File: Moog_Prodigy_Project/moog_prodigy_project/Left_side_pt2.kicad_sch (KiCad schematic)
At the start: 61 parts, among them Q1 CA3046, Q15 BC549, Q2 CA3046, Q4 CA3046, Q6 BC549, SW1 Switch_4x4, SW4 Switch_4x4, U2A1 OPA134, U2B3 OPA134, U5 NE5532, U6 LT1011CN8, U7 AD8066ARM, U8 NE5532

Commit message: Spajanje projekta final 1
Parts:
- removed C1, C9: 47p, Capacitor_THT:CP_Radial_D5.0mm_P2.50mm, symbol Device:C
- removed C10, C5, C6: 10n, Capacitor_THT:C_Disc_D3.8mm_W2.6mm_P2.50mm, symbol Device:C
- removed C11: 0.5n, Capacitor_THT:C_Disc_D3.8mm_W2.6mm_P2.50mm, symbol Device:C
- removed C12: 0.01n, Capacitor_THT:C_Disc_D3.8mm_W2.6mm_P2.50mm, symbol Device:C
- removed C2: 0.01, Capacitor_THT:C_Disc_D3.8mm_W2.6mm_P2.50mm, symbol Device:C
- removed C7: 1000n, Capacitor_THT:CP_Radial_D5.0mm_P2.50mm, symbol Device:C
- removed C8: 1n, Capacitor_THT:C_Disc_D3.8mm_W2.6mm_P2.50mm, symbol Device:C
- removed Q1, Q2, Q4, UI2: CA3046, CA3046:DIL14, symbol CA3046:CA3046
- removed Q14: ~, BF256C:TO92127P478H483-3, symbol Transistor_FET:BF256C
- removed Q15, Q6: BC549, Package_TO_SOT_THT:TO-92_Inline, symbol Transistor_BJT:BC549
- removed R1, R2: 2M, Resistor_THT:R_Axial_DIN0207_L6.3mm_D2.5mm_P7.62mm_Horizontal, symbol Device:R
- removed R10: 1K, Resistor_THT:R_Axial_DIN0207_L6.3mm_D2.5mm_P7.62mm_Horizontal, symbol Device:R
- removed R11: 12K, Resistor_THT:R_Axial_DIN0207_L6.3mm_D2.5mm_P7.62mm_Horizontal, symbol Device:R
- removed R12, R51, R8: 100K, Resistor_THT:R_Axial_DIN0207_L6.3mm_D2.5mm_P7.62mm_Horizontal, symbol Device:R
- removed R13: 63K4, Resistor_THT:R_Axial_DIN0207_L6.3mm_D2.5mm_P7.62mm_Horizontal, symbol Device:R
- removed R14, R7: 500, Resistor_THT:R_Axial_DIN0207_L6.3mm_D2.5mm_P7.62mm_Horizontal, symbol Device:R_Potentiometer
- removed R15: 3K, Resistor_THT:R_Axial_DIN0207_L6.3mm_D2.5mm_P7.62mm_Horizontal, symbol Device:R
- removed R16: 22K, Resistor_THT:R_Axial_DIN0207_L6.3mm_D2.5mm_P7.62mm_Horizontal, symbol Device:R
- removed R17: 15K, Resistor_THT:R_Axial_DIN0207_L6.3mm_D2.5mm_P7.62mm_Horizontal, symbol Device:R
- removed R18: 470, Resistor_THT:R_Axial_DIN0207_L6.3mm_D2.5mm_P7.62mm_Horizontal, symbol Device:R
- removed R3, R42, R54: 10K, Resistor_THT:R_Axial_DIN0207_L6.3mm_D2.5mm_P7.62mm_Horizontal, symbol Device:R_Potentiometer
- removed R4: 120K, Resistor_THT:R_Axial_DIN0207_L6.3mm_D2.5mm_P7.62mm_Horizontal, symbol Device:R
- removed R40: 20K, Resistor_THT:R_Axial_DIN0207_L6.3mm_D2.5mm_P7.62mm_Horizontal, symbol Device:R
- removed R41, R43: 2K, Resistor_THT:R_Axial_DIN0207_L6.3mm_D2.5mm_P7.62mm_Horizontal, symbol Device:R
- removed R44: 1M, Resistor_THT:R_Axial_DIN0207_L6.3mm_D2.5mm_P7.62mm_Horizontal, symbol Device:R
- removed R45, R46, R47, R48, R49, R50, R52, R55, R56: 10K, Resistor_THT:R_Axial_DIN0207_L6.3mm_D2.5mm_P7.62mm_Horizontal, symbol Device:R
- removed R5, R6: 100, Resistor_THT:R_Axial_DIN0207_L6.3mm_D2.5mm_P7.62mm_Horizontal, symbol Device:R
- removed R53: 51M, Resistor_THT:R_Axial_DIN0207_L6.3mm_D2.5mm_P7.62mm_Horizontal, symbol Device:R
- removed R57: 18K2, Resistor_THT:R_Axial_DIN0207_L6.3mm_D2.5mm_P7.62mm_Horizontal, symbol Device:R
- removed R9: 4K75, Resistor_THT:R_Axial_DIN0207_L6.3mm_D2.5mm_P7.62mm_Horizontal, symbol Device:R
- removed SW1, SW4: Switch_4x4, SLW-1575662-5A-S-D_Switch_4x4:SW_SLW-1575662-5A-S-D, symbol Power_supply:SW_Slide_DPDT_4x4
- removed U2A1, U2B3: OPA134, OPA134PA:DIP794W45P254L959H508Q8, symbol Amplifier_Operational:OPA134
- removed U5, U8: NE5532, NE5532AP:DIP794W45P254L1016H508Q8, symbol Amplifier_Operational:NE5532
- removed U6: LT1011CN8, Package_DIP:DIP-8_W7.62mm_Socket, symbol LM393BIPWR:LM393BIPWR
- removed U7: AD8066ARM, AD8066ARM:SOP65P490X110-8N, symbol AD8066ARM:AD8066ARM
- added C13, C16, C17, C18, C4: 10n, Capacitor_THT:C_Disc_D3.8mm_W2.6mm_P2.50mm, symbol Device:C
- added C14: 1n, Capacitor_THT:C_Disc_D3.8mm_W2.6mm_P2.50mm, symbol Device:C
- added C15, C3: 47p, Capacitor_THT:CP_Radial_D5.0mm_P2.50mm, symbol Device:C
- added C19: 500p, Capacitor_THT:CP_Radial_D5.0mm_P2.50mm, symbol Device:C
- added C20: 0.01n, Capacitor_THT:C_Disc_D3.8mm_W2.6mm_P2.50mm, symbol Device:C
- added LED1: ~, WP7113LGD:LED_WP7113LGD, symbol Device:LED_DIODA
- added Q1, Q2, UI3: CA3046, CA3046:DIL14, symbol CA3046:CA3046
- added Q11: BC107, Package_TO_SOT_THT:TO-18-3, symbol Transistor_BJT:BC107
- added Q13, Q16: ~, BF256C:TO92127P478H483-3, symbol Transistor_FET:BF256C
- added Q17: BC549, Package_TO_SOT_THT:TO-92_Inline, symbol Transistor_BJT:BC549
- added R171, R21, R23, R63, R69: 10K, Resistor_THT:R_Axial_DIN0207_L6.3mm_D2.5mm_P7.62mm_Horizontal, symbol Device:R_Potentiometer
- added R19, R20, R61: 1M, Resistor_THT:R_Axial_DIN0207_L6.3mm_D2.5mm_P7.62mm_Horizontal, symbol Device:R
- added R22: 82K, Resistor_THT:R_Axial_DIN0207_L6.3mm_D2.5mm_P7.62mm_Horizontal, symbol Device:R
- added R24: 120K, Resistor_THT:R_Axial_DIN0207_L6.3mm_D2.5mm_P7.62mm_Horizontal, symbol Device:R
- added R25: 10, Resistor_THT:R_Axial_DIN0207_L6.3mm_D2.5mm_P7.62mm_Horizontal, symbol Device:R
- added R26, R27: 100, Resistor_THT:R_Axial_DIN0207_L6.3mm_D2.5mm_P7.62mm_Horizontal, symbol Device:R
- added R28, R35: 500, Resistor_THT:R_Axial_DIN0207_L6.3mm_D2.5mm_P7.62mm_Horizontal, symbol Device:R_Potentiometer
- added R30: 4K75, Resistor_THT:R_Axial_DIN0207_L6.3mm_D2.5mm_P7.62mm_Horizontal, symbol Device:R
- added R31, R76: 1K, Resistor_THT:R_Axial_DIN0207_L6.3mm_D2.5mm_P7.62mm_Horizontal, symbol Device:R
- added R32: 12KΩ, Resistor_THT:R_Axial_DIN0207_L6.3mm_D2.5mm_P7.62mm_Horizontal, symbol Device:R
- added R33: 100KΩ, Resistor_THT:R_Axial_DIN0207_L6.3mm_D2.5mm_P7.62mm_Horizontal, symbol Device:R
- added R34, R73: 100K, Resistor_THT:R_Axial_DIN0207_L6.3mm_D2.5mm_P7.62mm_Horizontal, symbol Device:R
- added R36: 3K, Resistor_THT:R_Axial_DIN0207_L6.3mm_D2.5mm_P7.62mm_Horizontal, symbol Device:R
- added R37: 22K, Resistor_THT:R_Axial_DIN0207_L6.3mm_D2.5mm_P7.62mm_Horizontal, symbol Device:R
- added R38: 15K, Resistor_THT:R_Axial_DIN0207_L6.3mm_D2.5mm_P7.62mm_Horizontal, symbol Device:R
- added R39: 470, Resistor_THT:R_Axial_DIN0207_L6.3mm_D2.5mm_P7.62mm_Horizontal, symbol Device:R
- added R58: 20K, Resistor_THT:R_Axial_DIN0207_L6.3mm_D2.5mm_P7.62mm_Horizontal, symbol Device:R
- added R59: 560, Resistor_THT:R_Axial_DIN0207_L6.3mm_D2.5mm_P7.62mm_Horizontal, symbol Device:R
- added R60: 2K, Resistor_THT:R_Axial_DIN0207_L6.3mm_D2.5mm_P7.62mm_Horizontal, symbol Device:R
- added R62, R64, R65, R66, R67, R68, R70, R71, R74, R75: 10K, Resistor_THT:R_Axial_DIN0207_L6.3mm_D2.5mm_P7.62mm_Horizontal, symbol Device:R
- added R72: 5.1M, Resistor_THT:R_Axial_DIN0207_L6.3mm_D2.5mm_P7.62mm_Horizontal, symbol Device:R
- added S4-1, S4-2: SW_SPST, L101011ML04Q_1x1:SW_L101011ML04Q, symbol Switch:SW_SPST
- added SW2, SW5: Switch_4x4, SLW-1575662-5A-S-D_Switch_4x4:SW_SLW-1575662-5A-S-D, symbol Power_supply:SW_Slide_DPDT_4x4
- added SW3: SW_Slide_DPDT_3x3, CL-SB-22A-02T_3x3:SW_CL-SB-22A-02T, symbol Switch:SW_Slide_DPDT
- added U1: NE5532, NE5532AP:DIP794W45P254L1016H508Q8, symbol Amplifier_Operational:NE5532
- added U10: AD8066ARM, AD8066ARM:SOP65P490X110-8N, symbol AD8066ARM:AD8066ARM
- added U2B1, U4B1: OPA134, OPA134PA:DIP794W45P254L959H508Q8, symbol Amplifier_Operational:OPA134
- added U9: LT1011CN8, Package_DIP:DIP-8_W7.62mm_Socket, symbol LM393BIPWR:LM393BIPWR
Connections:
- net +12V: now also C16.2, Q1.8, R171.1, R21.1, R23.1, R33.1, R34.1, R58.2, R70.2, SW2.2 (B), SW2.4 (D), U10.4, U2B1.7 (V+), U4B1.7 (V+), U9.8
- net -12V: now also C17.1, Q11.1 (E), R171.3, R21.3, R23.3, R32.1, R38.1, S4-1.2 (B), SW3.6 (C), U10.8, U2B1.4 (V-), U4B1.4 (V-), U9.4
- net Flag_ka_U6A: now also SW3.4 (A)
- net GND: now also C13.1, C16.1, C17.2, C18.1, C19.1, Q1.6, Q2.13, R26.2, R27.1, R31.1, R36.2, R59.2, R62.2, R69.3, R74.2, R75.1, U2B1.3 (+)
- new net: Q2.12, R33.2, U4B1.3 (+)
- new net: R21.2, R22.1
- new net: R22.2, R24.2, R25.1, R26.1, UI3.2
- new net: R59.1, R76.2
- new net: C15.1, Q16.2 (G), R60.1, R61.1, U9.1
- new net: C15.2, R61.2, R62.1, U9.3
- new net: Q17.3 (E), R64.1, R73.2, R74.1, SW5.1 (A), U10.2
- new net: R64.2, U9.2
- new net: R28.1, R28.2, R30.2
- new net: R27.2, R28.3, UI3.4
- new net: C14.1, Q13.3 (S), Q16.1 (D), R63.1, R63.2
- new net: C14.2, Q13.1 (D), Q16.3 (S), R60.2, U1.1, U1.2 (-)
- new net: C13.2, C18.2, R58.1, R75.2, U1.3 (+), U9.6
- new net: Q13.2 (G), SW3.5 (B)
- new net: Q17.1 (C), R65.1, R67.1
- new net: C19.2, R67.2, U1.5 (+)
- new net: R66.2, R68.1, U1.6 (-)
- new net: R68.2, R69.1, SW5.6 (F), U1.7
- new net: LED1.1, S4-1.1 (A)
- new net: C4.2, R37.1, U4B1.6
- new net: Q11.2 (B), R37.2, R38.2
- new net: R25.2, SW3.3 (C)
- new net: Q1.10, R31.2, R32.2
- new net: R63.3, U10.3, UI3.1
- new net: C3.1, U2B1.6, UI3.3
- new net: C3.2, R20.2, SW2.5 (E), U2B1.2 (-), UI3.5
- new net: C4.1, R35.2, U4B1.2 (-)
- new net: R65.2, R66.1
- new net: R35.3, R36.1
- new net: LED1.2, S4-2.1 (A)
- new net: R76.1, S4-2.2 (B)
- new net: C20.1, R71.1, R72.2, U9.7
- new net: R70.1, R71.2, SW5.4 (D)
- new net: R34.2, R35.1
- new net: R19.1, R20.1, SW2.3 (C)
- new net: Q17.2 (B), U10.1
- new net: R19.2, SW2.1 (A), SW2.6 (F)
- new net: R171.2, SW3.2 (B)
- new net: Q11.3 (C), R39.1
- new net: Q1.7, R39.2
- new net: R23.2, R24.1
- new net: C20.2, R72.1, R73.1, U9.5
- new net: SW5.2 (B), SW5.3 (C), SW5.7 (G)
- new net Diodna zastita izlaz iz R86: R30.1
- new net Flag_ka_R94: R69.2
- new net Ulaz_na_diodnu_zastitu: SW3.1 (A)
- no-connect marks 9 -> 11
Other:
- note added: "HI END ADJUST"
- note added: "INTERVAL"
- note added: "OSC 2 FREQ TRIM"
- note added: "OSC 2 LEVEL"
- note added: "OSC 2 SCALE TRIM"
- note added: "PITCH (SYNC)"
- note added: "SYNC SWITCH"
- note removed: "OSC 1 CHIP TEMP TRIM"
- note removed: "OSC 1 FREQ TRIM"
- note removed: "OSC 1 HIGH END TRIM"
- note removed: "OSC 1 LEVEL"
- note removed: "OSC 1 SCALE TRIM"
- note removed: "Q2"
- note removed: "Q3"

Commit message: PCB priprema i fix gresaka
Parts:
- added unit 3 of U1
- LED1: value ~ -> Led_dioda; footprint WP7113LGD:LED_WP7113LGD -> LED_THT:LED_D5.0mm
- R21, R63: footprint Resistor_THT:R_Axial_DIN0207_L6.3mm_D2.5mm_P7.62mm_Horizontal -> Potentiometer_THT:Potentiometer_ACP_CA9-V10_Vertical
- RV171: renamed from R171; footprint Resistor_THT:R_Axial_DIN0207_L6.3mm_D2.5mm_P7.62mm_Horizontal -> Potentiometer_THT:Potentiometer_Bourns_3339P_Vertical_HandSoldering
- RV23: renamed from R23; footprint Resistor_THT:R_Axial_DIN0207_L6.3mm_D2.5mm_P7.62mm_Horizontal -> Potentiometer_THT:Potentiometer_Bourns_3339P_Vertical_HandSoldering
- RV28: renamed from R28; footprint Resistor_THT:R_Axial_DIN0207_L6.3mm_D2.5mm_P7.62mm_Horizontal -> Potentiometer_THT:Potentiometer_Bourns_3339P_Vertical_HandSoldering
- RV35: renamed from R35; footprint Resistor_THT:R_Axial_DIN0207_L6.3mm_D2.5mm_P7.62mm_Horizontal -> Potentiometer_THT:Potentiometer_Bourns_3339P_Vertical_HandSoldering
- RV69: renamed from R69; footprint Resistor_THT:R_Axial_DIN0207_L6.3mm_D2.5mm_P7.62mm_Horizontal -> Potentiometer_THT:Potentiometer_Bourns_3339P_Vertical_HandSoldering
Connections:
- net +12V: now also U1.8 (V+)
- net -12V: now also U1.4 (V-)

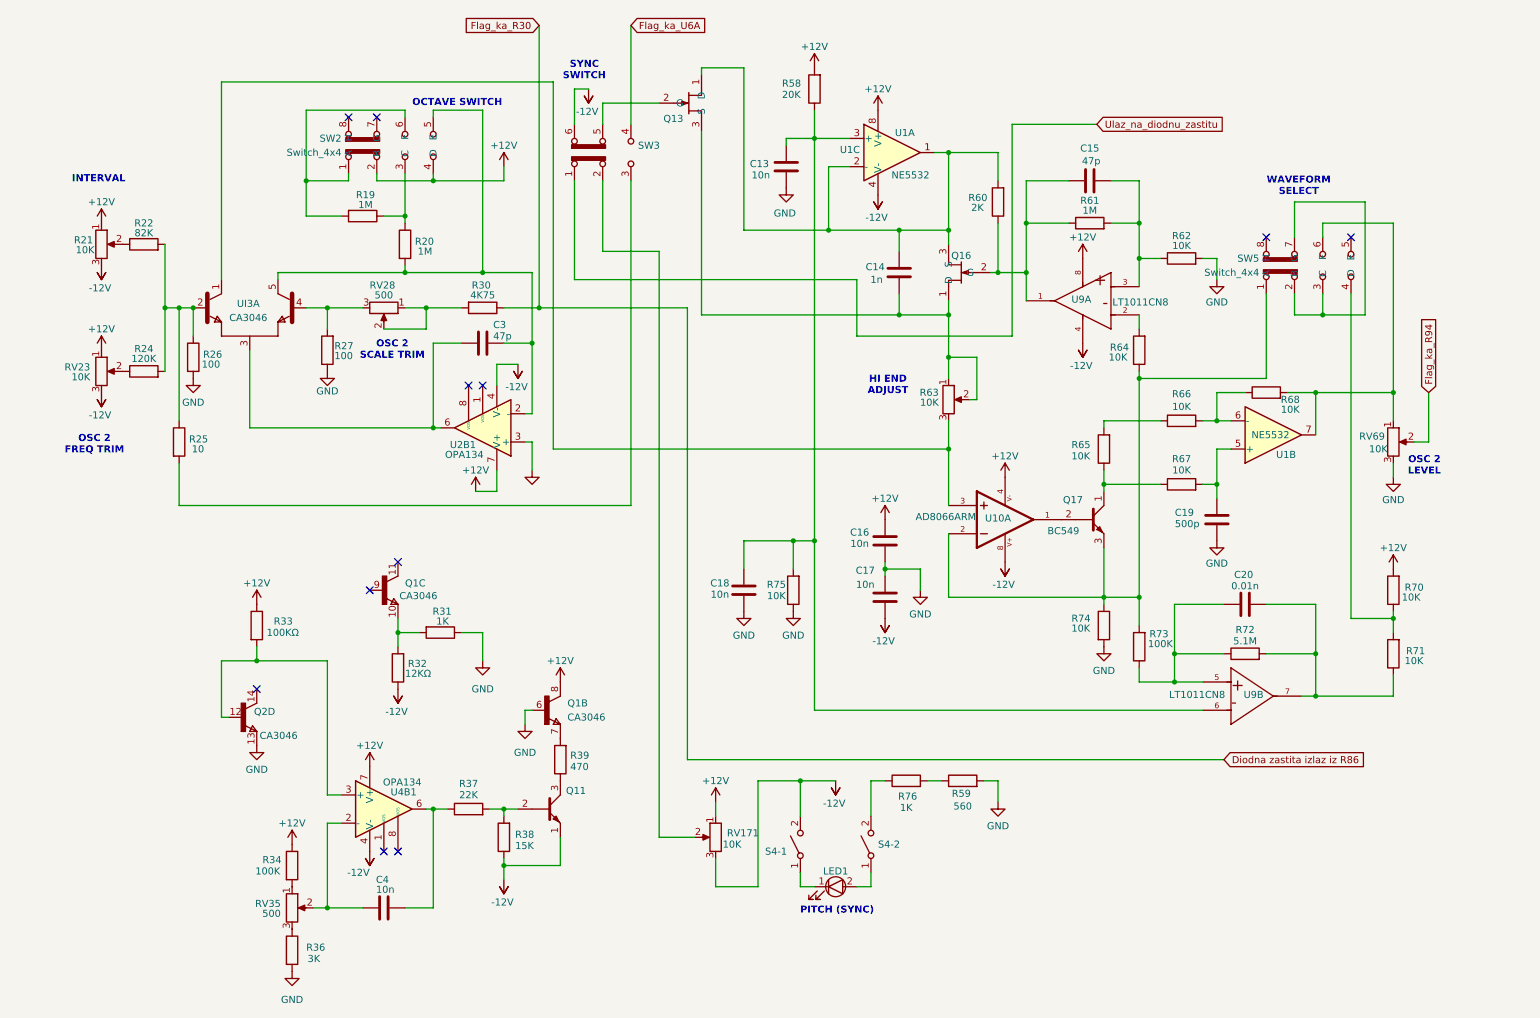
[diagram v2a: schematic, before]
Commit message: problemi sa ca3096, multiplicirani footprintovi
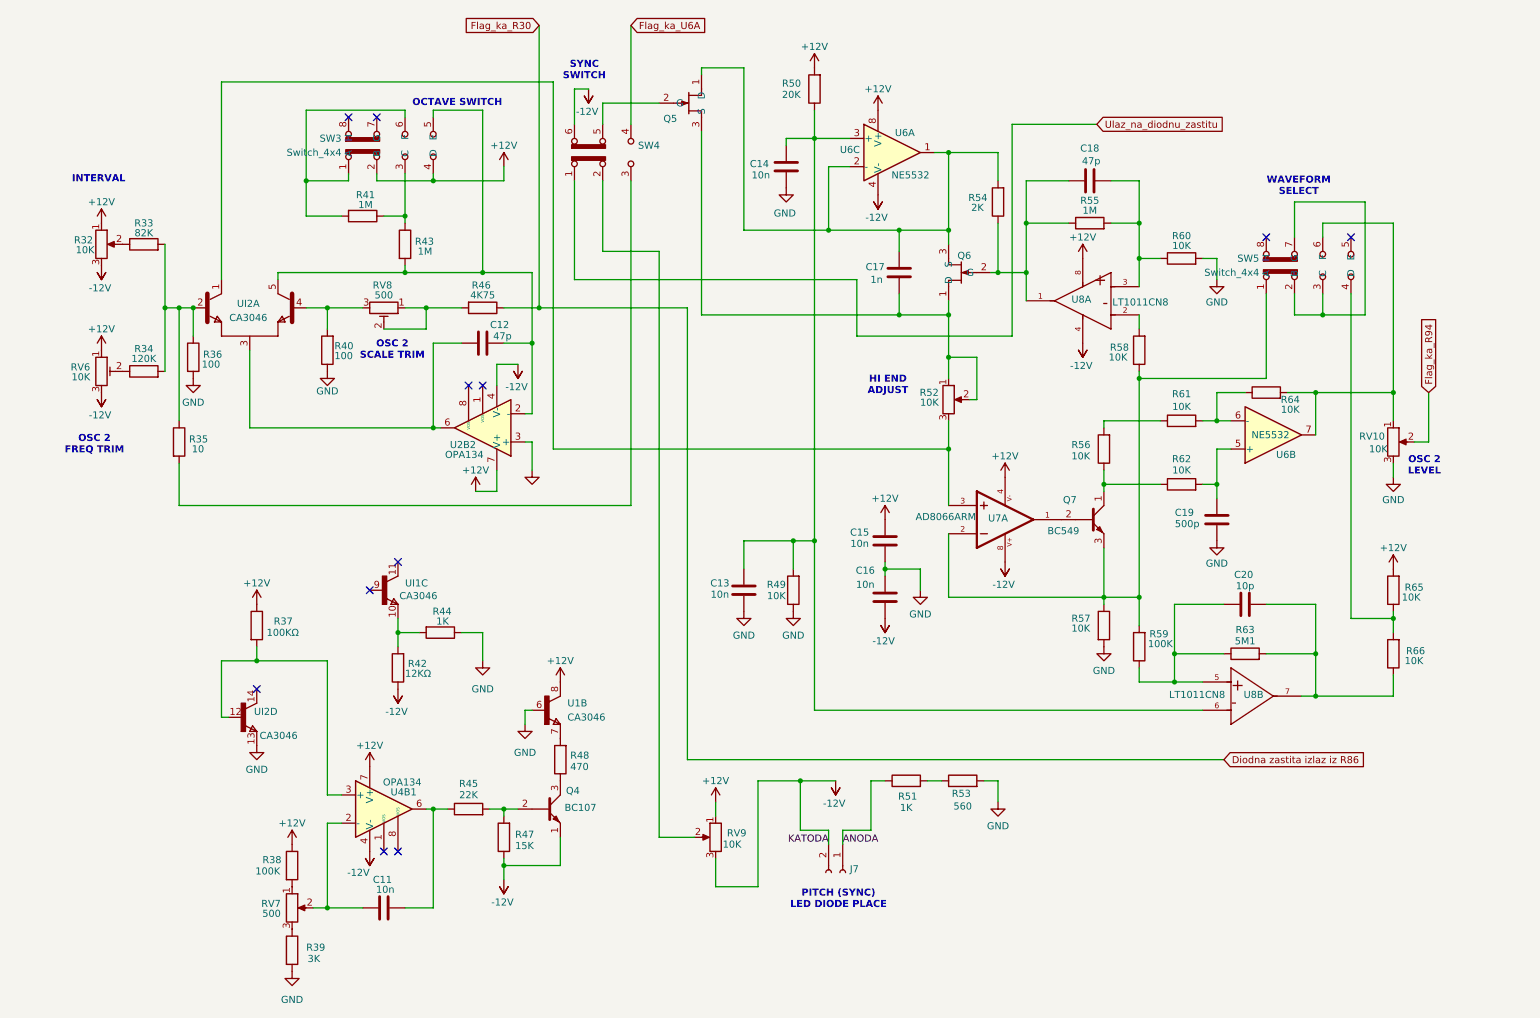
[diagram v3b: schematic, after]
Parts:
- removed LED1: Led_dioda, LED_THT:LED_D5.0mm, symbol Device:LED_DIODA
- removed S4-1, S4-2: SW_SPST, L101011ML04Q_1x1:SW_L101011ML04Q, symbol Switch:SW_SPST
- added J7: Conn_01x02_Socket, Connector_PinSocket_2.54mm:PinSocket_1x02_P2.54mm_Vertical, symbol Connector:Conn_01x02_Socket
- C20: value 0.01n -> 10p
- R63: renamed from R72; value 5.1M -> 5M1
- RV6: renamed from RV23; symbol Device:R_Potentiometer -> Device:R_Potentiometer_Trim
- RV8: renamed from RV28; symbol Device:R_Potentiometer -> Device:R_Potentiometer_Trim
- SW4: renamed from SW3; footprint CL-SB-22A-02T_3x3:SW_CL-SB-22A-02T -> Button_Switch_THT:SW_CK_JS202011CQN_DPDT_Straight
- U7: renamed from U10; footprint AD8066ARM:SOP65P490X110-8N -> Package_DIP:DIP-8_W7.62mm_Socket
- renumbered C4 to C11, C3 to C12, C18 to C13, C13 to C14, C16 to C15, C17 to C16, C14 to C17, C15 to C18, Q11 to Q4, Q13 to Q5, Q16 to Q6, Q17 to Q7, R21 to R32, R22 to R33, R24 to R34, R25 to R35, R26 to R36, R33 to R37, R34 to R38, R36 to R39, R27 to R40, R19 to R41, R32 to R42, R20 to R43, R31 to R44, R37 to R45, R30 to R46, R38 to R47, R39 to R48, R75 to R49, R58 to R50, R76 to R51, R63 to R52, R59 to R53, R60 to R54, R61 to R55, R65 to R56, R74 to R57, R64 to R58, R73 to R59, R62 to R60, R66 to R61, R67 to R62, R68 to R64, R70 to R65, R71 to R66, RV69 to RV10, RV35 to RV7, RV171 to RV9, SW2 to SW3, Q1 to U1, U2B1 to U2B2, U1 to U6, U9 to U8, Q1 to UI1, UI3 to UI2, Q2 to UI2
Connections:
- net -12V: now also J7.2 (KATODA)
- net ANODA: now reaches R51.1
- net ANODA: now also J7.1 (ANODA)
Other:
- note added: "PITCH (SYNC) LED DIODE PLACE"
- note removed: "PITCH (SYNC)"

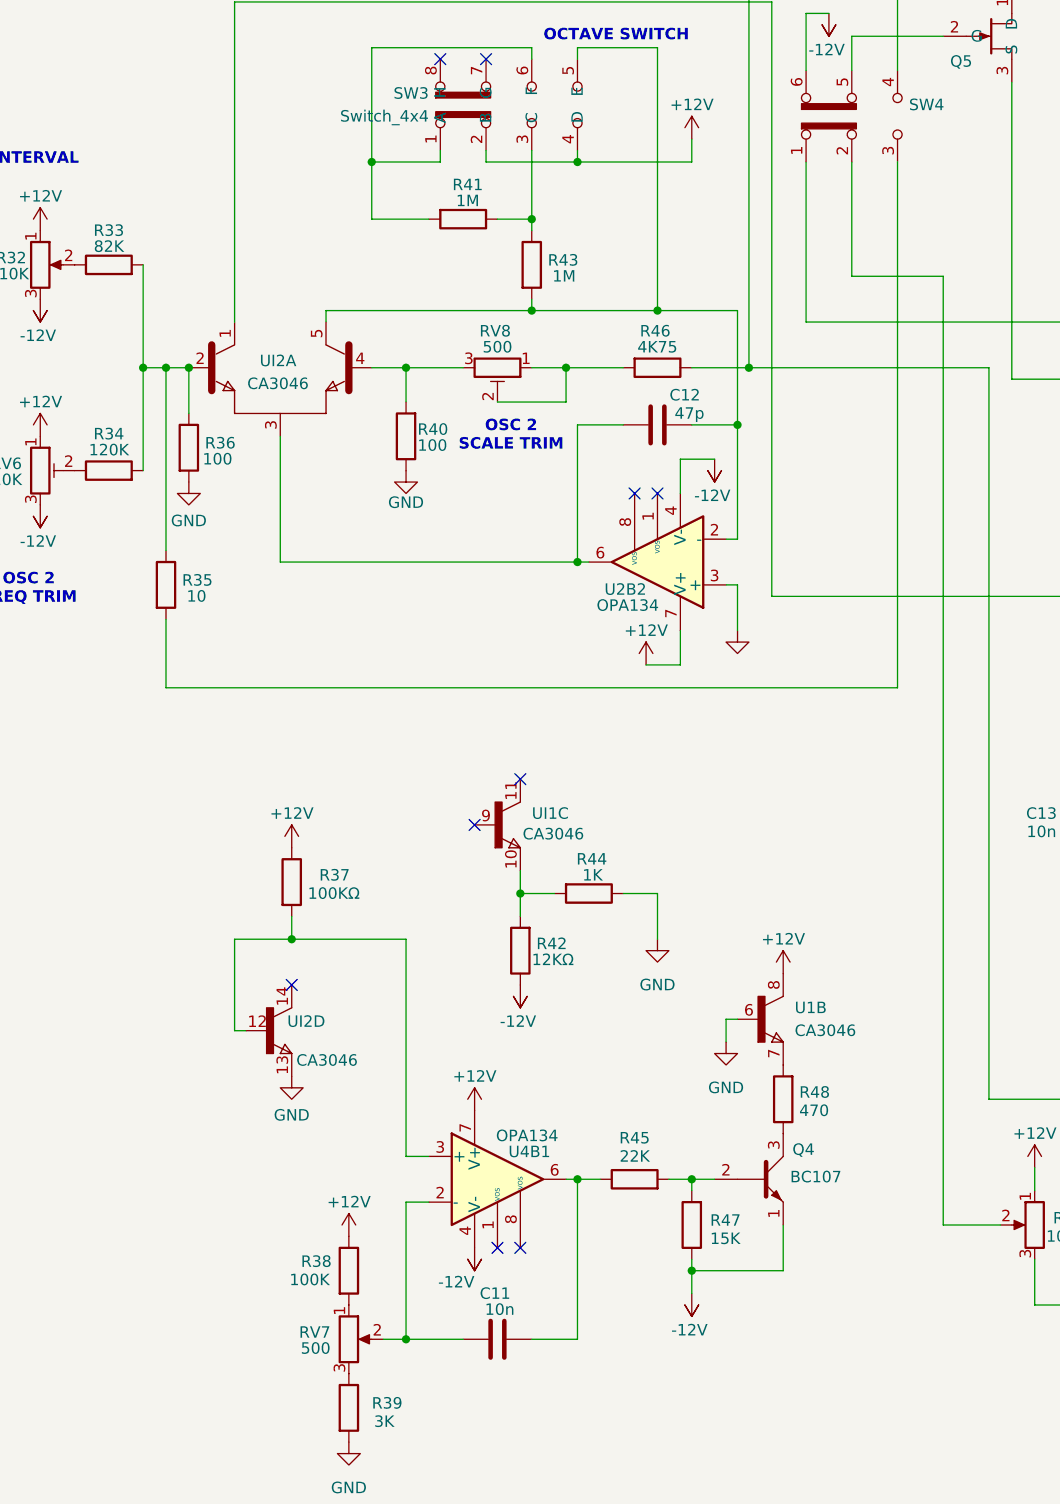
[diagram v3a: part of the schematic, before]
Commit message: CA3046 leva strana seme update
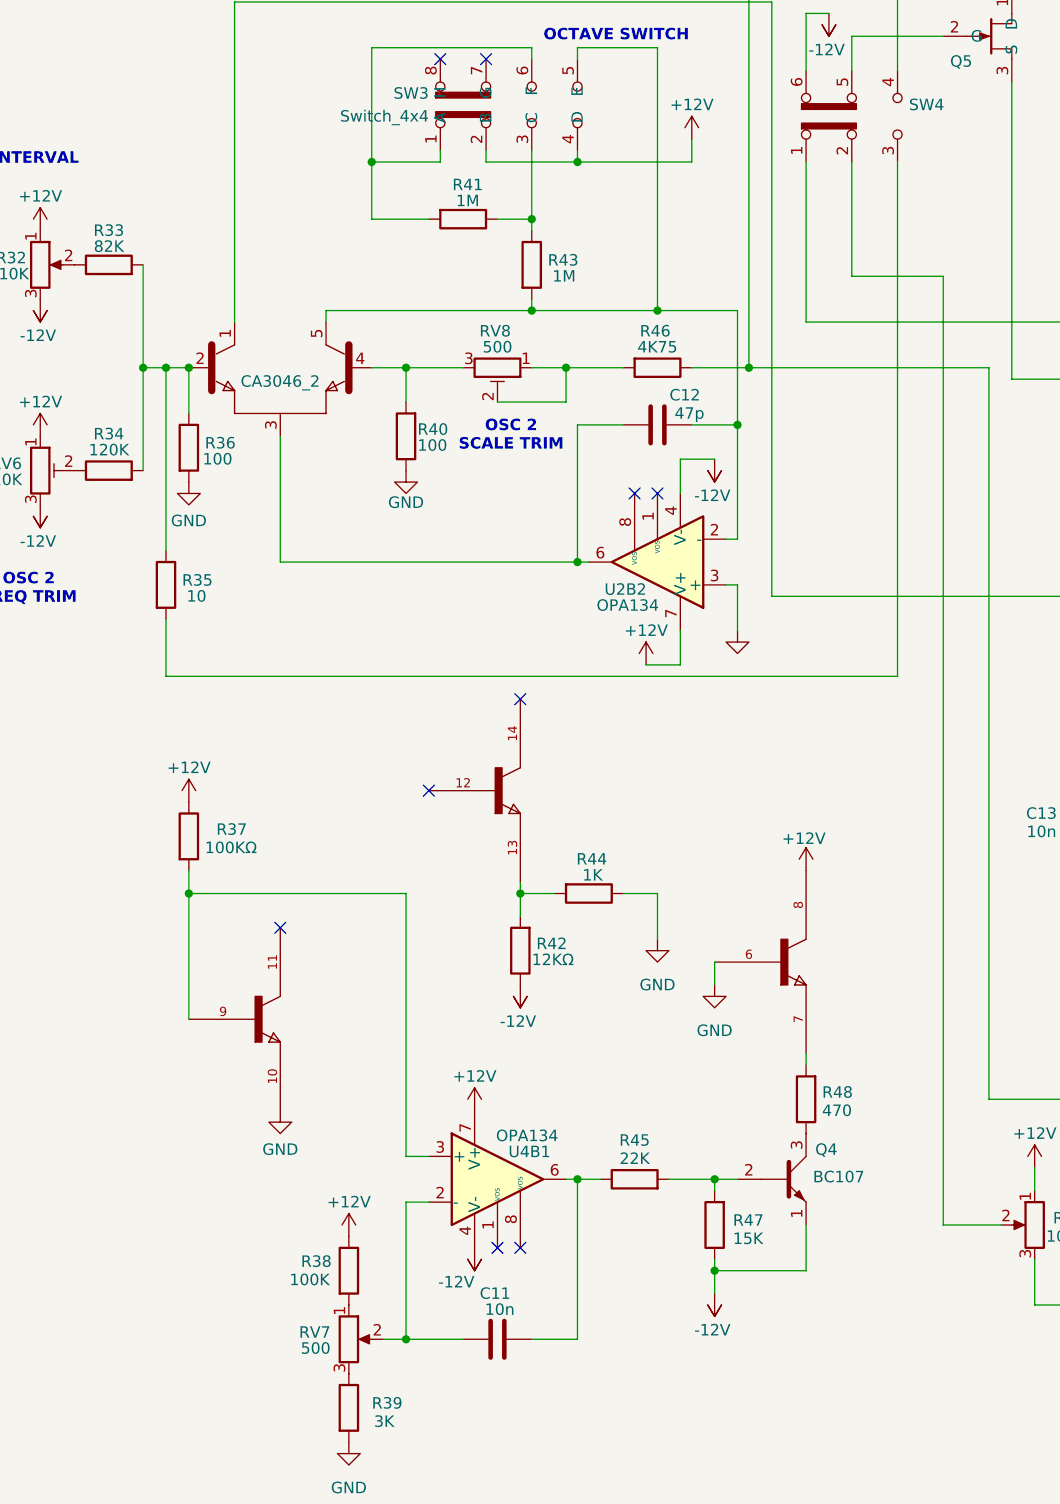
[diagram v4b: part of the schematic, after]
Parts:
- removed U1, UI1, UI2: CA3046, CA3046:DIL14, symbol CA3046:CA3046
- added CA3046_2: CA3046_2, CA3046:DIL14, symbol CA3046:CA3046_novi_2
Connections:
- net +12V: now also CA3046_2.8
- net GND: now also CA3046_2.10, CA3046_2.6
- net at R37.2, U4B1.3 (+): now also CA3046_2.9
- net at R33.2, R34.2, R35.1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: now also CA3046_2.2
- net at R40.2, RV8.3: now also CA3046_2.4
- net at R42.2, R44.2: now also CA3046_2.13
- net at R52.3, U7.3: now also CA3046_2.1
- net at C12.1, U2B2.6: now also CA3046_2.3
- net at C12.2, R43.2, SW3.5 (E)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: now also CA3046_2.5
- net at R48.2: now also CA3046_2.7
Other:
- moved on the sheet: Q4, R37, R47, R48
